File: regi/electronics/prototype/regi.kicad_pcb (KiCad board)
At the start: 2 copper layers, 70.3 x 67.5 mm, 86 parts, among them J1 USB2UART, J2 1.47 IPS LCD, J3 ConnBattery, J4 RTD_PT100, Q1 SS8050, Q2 SS8050, Q3 SS8050, Q5 SS8050, SW1 RST, SW2 IN1, SW3 Boot, SW4 IN2, SW5 IN4, SW6 IN4, SW7 IN5, U1 CH340C, U2 ESP32-S3-WROOM-1, U3 TPS63001_SEPIC_3V3, U4 MAX31865xTP, U5 BQ24075RGT_DPPM, U7 BQ27421YZFR-G1A

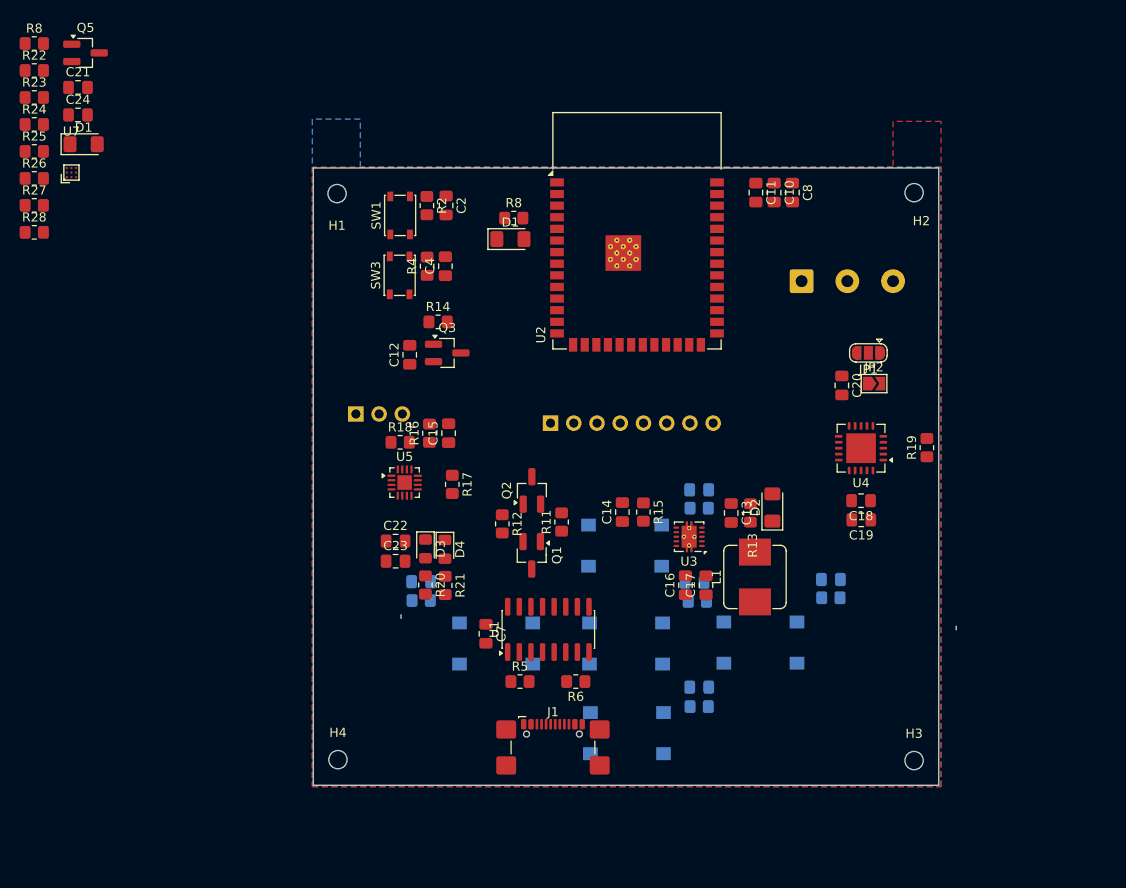
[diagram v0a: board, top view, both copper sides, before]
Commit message: feat(regi): finished rough routing
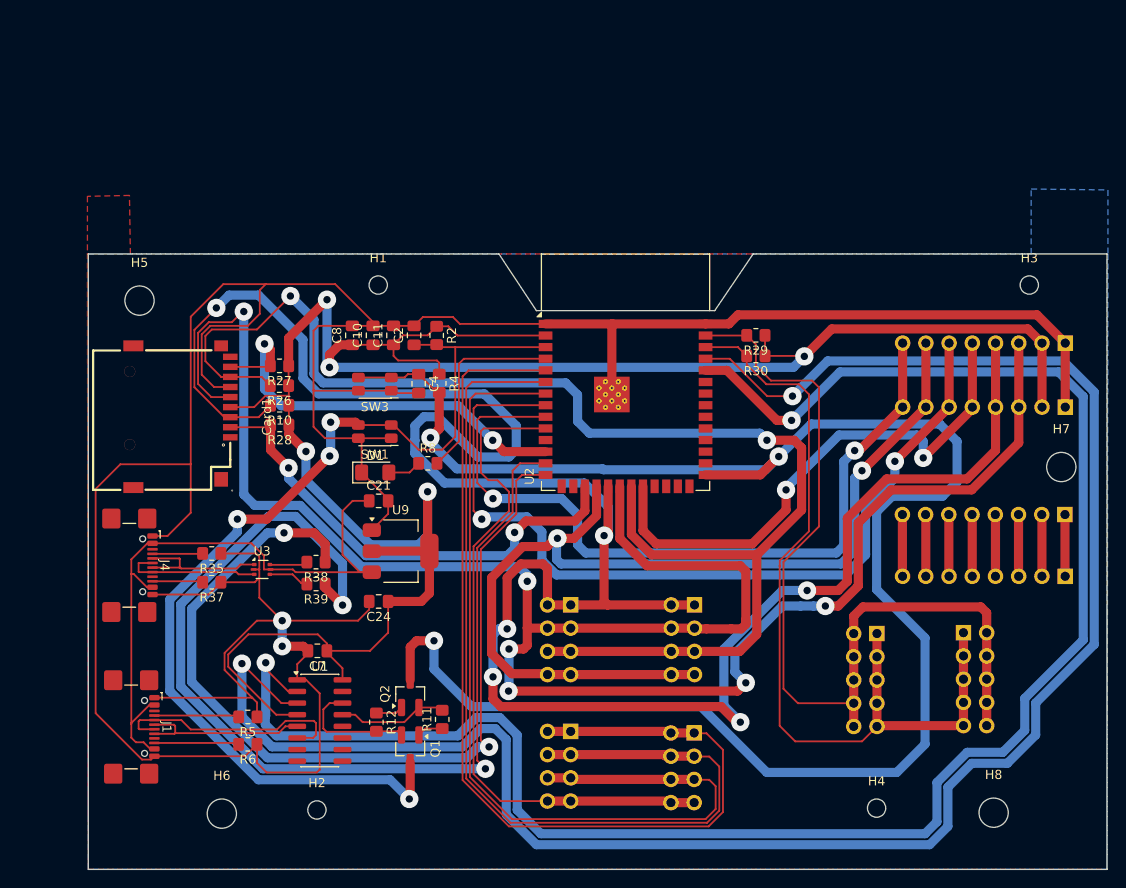
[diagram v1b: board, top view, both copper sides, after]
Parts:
- removed C1, C12, C18, C19, C20, C3, C5, C6, C9: 100nF, Capacitor_SMD:C_0805_2012Metric_Pad1.18x1.45mm_HandSolder
- removed C13, C16, C17: 10uF, Capacitor_SMD:C_0805_2012Metric_Pad1.18x1.45mm_HandSolder
- removed C14: 0.1uF, Capacitor_SMD:C_0805_2012Metric_Pad1.18x1.45mm_HandSolder
- removed C15: 1uF, Capacitor_SMD:C_0805_2012Metric_Pad1.18x1.45mm_HandSolder
- removed C22, C23: 4.7uF, Capacitor_SMD:C_0805_2012Metric_Pad1.18x1.45mm_HandSolder
- removed the D1 at (76.5, 65.0)
- removed the D1 at (123.2, 75.4)
- removed D2: VDD, LED_SMD:LED_1206_3216Metric_Pad1.42x1.75mm_HandSolder
- removed D3: green, LED_SMD:LED_0805_2012Metric_Pad1.15x1.40mm_HandSolder
- removed D4: red, LED_SMD:LED_0805_2012Metric_Pad1.15x1.40mm_HandSolder
- removed JP1: 3_OR_2_Wire, Jumper:SolderJumper-3_P1.3mm_Open_RoundedPad1.0x1.5mm
- removed JP2: 2_Wire, Jumper:SolderJumper-2_P1.3mm_Open_TrianglePad1.0x1.5mm
- removed L1: 22uH 1A, Inductor_SMD:L_Bourns_SRP7028A_7.3x6.6mm
- removed Q3, Q5: SS8050, Package_TO_SOT_SMD:SOT-23_Handsoldering
- removed R1, R13, R14, R3, R7, R9: 1k, Resistor_SMD:R_0805_2012Metric_Pad1.20x1.40mm_HandSolder
- removed R15: 100, Resistor_SMD:R_0805_2012Metric_Pad1.20x1.40mm_HandSolder
- removed R16: 46.4K, Resistor_SMD:R_0805_2012Metric_Pad1.20x1.40mm_HandSolder
- removed R17: 2K2, Resistor_SMD:R_0805_2012Metric_Pad1.20x1.40mm_HandSolder
- removed R18: 1.13k, Resistor_SMD:R_0805_2012Metric_Pad1.20x1.40mm_HandSolder
- removed R19: 430 1%, Resistor_SMD:R_0805_2012Metric_Pad1.20x1.40mm_HandSolder
- removed R20, R21: 1K5, Resistor_SMD:R_0805_2012Metric_Pad1.20x1.40mm_HandSolder
- removed R22, R23: 4K7, Resistor_SMD:R_0805_2012Metric_Pad1.20x1.40mm_HandSolder
- removed R24: 10k, Resistor_SMD:R_0805_2012Metric_Pad1.20x1.40mm_HandSolder
- removed R25: 10K, Resistor_SMD:R_0805_2012Metric_Pad1.20x1.40mm_HandSolder
- removed the R8 at (71.1, 54.0)
- removed the R8 at (123.5, 73.1)
- removed SW2: IN1, Button_Switch_SMD:SW_SPST_Omron_B3FS-100xP
- removed SW4: IN2, Button_Switch_SMD:SW_SPST_Omron_B3FS-100xP
- removed SW5, SW6: IN4, Button_Switch_SMD:SW_SPST_Omron_B3FS-100xP
- removed SW7: IN5, Button_Switch_SMD:SW_SPST_Omron_B3FS-100xP
- removed U4: MAX31865xTP, Package_DFN_QFN:TQFN-20-1EP_5x5mm_P0.65mm_EP3.25x3.25mm
- removed U5: BQ24075RGT_DPPM, Package_DFN_QFN:VQFN-16-1EP_3x3mm_P0.5mm_EP1.6x1.6mm
- removed U7: BQ27421YZFR-G1A, easyeda2kicad:DSBGA-9_L1.5-W1.5-R3-C3-P0.50-BL
- added Card1: TF PUSH, easyeda2kicad:TF-SMD_TF-PUSH, F.Cu at (87.2, 94.8)
- added D1: Indicator, LED_SMD:LED_1206_3216Metric_Pad1.42x1.75mm_HandSolder, F.Cu at (108.4, 100.9)
- added H5: MountingHole, MountingHole:MountingHole_3.2mm_M3, F.Cu at (82.6, 82.1)
- added H6: MountingHole, MountingHole:MountingHole_3.2mm_M3, F.Cu at (91.6, 138.2)
- added H7: MountingHole, MountingHole:MountingHole_3.2mm_M3, F.Cu at (183.4, 100.3)
- added H8: MountingHole, MountingHole:MountingHole_3.2mm_M3, F.Cu at (176.0, 138.1)
- added J10: PinHeaderSPI2, Connector_PinHeader_2.54mm:PinHeader_2x04_P2.54mm_Vertical, B.Cu at (129.8, 129.2)
- added J11: PinSocketSPI1, Connector_PinHeader_2.54mm:PinHeader_2x04_P2.54mm_Vertical, B.Cu at (143.3, 115.4)
- added J12: PinSocketSPI2, Connector_PinHeader_2.54mm:PinHeader_2x04_P2.54mm_Vertical, B.Cu at (143.2, 129.4)
- added J5: lcd jumper, Connector_PinHeader_2.54mm:PinHeader_1x08_P2.54mm_Vertical, B.Cu at (183.8, 86.8)
- added J6: lcd jumper, Connector_PinHeader_2.54mm:PinHeader_1x08_P2.54mm_Vertical, B.Cu at (183.8, 112.2)
- added J7: lcd jumper, Connector_PinHeader_2.54mm:PinHeader_1x08_P2.54mm_Vertical, B.Cu at (183.8, 105.5)
- added J8: PinSocketI2C, Connector_PinSocket_2.54mm:PinSocket_2x05_P2.54mm_Vertical, B.Cu at (172.7, 118.4)
- added J9: PinHeaderSPI1, Connector_PinHeader_2.54mm:PinHeader_2x04_P2.54mm_Vertical, B.Cu at (129.8, 115.4)
- added R29: 4K7, Resistor_SMD:R_0805_2012Metric_Pad1.20x1.40mm_HandSolder, F.Cu at (150.0, 85.9)
- added R30: 4K7, Resistor_SMD:R_0805_2012Metric_Pad1.20x1.40mm_HandSolder, F.Cu at (150.0, 88.2)
- added R35: 5K1, Resistor_SMD:R_0805_2012Metric_Pad1.20x1.40mm_HandSolder, F.Cu at (90.5, 109.8)
- added R37: 5K1, Resistor_SMD:R_0805_2012Metric_Pad1.20x1.40mm_HandSolder, F.Cu at (90.5, 112.9)
- added R38: 22 / 33, Resistor_SMD:R_0805_2012Metric_Pad1.20x1.40mm_HandSolder, F.Cu at (101.9, 110.7)
- added R39: 22 / 33, Resistor_SMD:R_0805_2012Metric_Pad1.20x1.40mm_HandSolder, F.Cu at (101.9, 113.1)
- added R8: 1k, Resistor_SMD:R_0805_2012Metric_Pad1.20x1.40mm_HandSolder, F.Cu at (114.1, 99.9)
- added U9: AMS1117-3.3, Package_TO_SOT_SMD:SOT-223-3_TabPin2, F.Cu at (111.2, 109.5)
- C21: value 0.47uF -> 22uF
- C24: value 100nF -> 22uF
- J3: value ConnBattery -> PinHeaderI2C; footprint Connector_PinHeader_2.54mm:PinHeader_1x03_P2.54mm_Vertical -> Connector_PinHeader_2.54mm:PinHeader_2x05_P2.54mm_Vertical
- J4: value RTD_PT100 -> USB2UART; footprint TerminalBlock_Phoenix:TerminalBlock_Phoenix_PT-1,5-3-5.0-H_1x03_P5.00mm_Horizontal -> Connector_USB:USB_C_Receptacle_GCT_USB4110; moved to F.Cu
- R10: value 1k -> 51k; moved to F.Cu
- R26: value 10K -> 51k
- R27: value 1k -> 51k
- R28: value 10k -> 51k
- SW1, SW3: footprint Button_Switch_SMD:SW_SPST_PTS810 -> Button_Switch_SMD:SW_SPST_EVQP7A
- U3: value TPS63001_SEPIC_3V3 -> USBLC6-2P6; footprint Package_SON:Texas_DRC0010J_ThermalVias -> Package_TO_SOT_SMD:SOT-666
- moved H2 93.9 mm to (102.0, 137.8)
- moved J4 80.9 mm to (80.3, 111.0), turned to -90 degrees
- moved C24 62.5 mm to (108.8, 115.0), turned to 180 degrees
- moved J3 61.8 mm to (163.2, 118.5), turned to 180 degrees
- moved H4 59.1 mm to (163.2, 137.6)
- moved J2 56.3 mm to (183.8, 93.8), turned to 90 degrees
- moved C21 55.9 mm to (108.8, 104.0)
- moved H3 53.5 mm to (179.9, 80.4)
- moved C8 50.6 mm to (105.9, 85.9), turned to 90 degrees
- moved R10 50.5 mm to (97.9, 93.5), turned to 180 degrees
- moved J1 47.4 mm to (80.5, 128.7), turned to -90 degrees
- moved U3 46.8 mm to (96.0, 111.5), turned to 0 degrees
- moved C10 46.6 mm to (108.1, 85.9), turned to 90 degrees
- moved C11 42.6 mm to (110.4, 85.9), turned to 90 degrees
- moved R6 36.5 mm to (94.4, 130.6)
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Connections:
- C21 pad 1: Net-(U7-VDD) -> VBUS
- C24 pad 1: /GPOUT -> +3.3V
- J3 pad 1: +BATT -> /I2C_SCL
- J3 pad 2: /TS -> /I2C_SDA
- J3 pad 3: GND -> /I2C_SCL
- R10 pad 2: /IN5 -> /MOSI
- R26 pad 1: /GPOUT -> +3.3V
- R26 pad 2: GND -> /MISO
- R27 pad 2: Net-(Q5-C) -> /MMC_INT
- R28 pad 2: Net-(Q5-B) -> /MMC_CS
- U2 pad 10: /IN1 -> /CS2
- U2 pad 11: /IN2 -> unconnected-(U2-IO18-Pad11)
- U2 pad 12: /MAX31865DRDY -> /MMC_INT
- U2 pad 13: /IN3 -> /USB_DM
- U2 pad 14: /IN4 -> /USB_DP
- U2 pad 17: /MAX31865CS -> /MMC_CS
- U2 pad 23: /IN5 -> unconnected-(U2-IO21-Pad23)
- U2 pad 31: Net-(Q3-E) -> unconnected-(U2-IO38-Pad31)
- U2 pad 32: /GPOUT -> unconnected-(U2-IO39-Pad32)
- U3 pad 1: +3.3V -> Net-(J4-D--PadA7)
- U3 pad 2: Net-(U3-L2) -> GND
- U3 pad 3: GND -> Net-(J4-D+-PadA6)
- U3 pad 5: VDD -> VBUS
- U3 pad 6: Net-(U3-EN) -> Net-(R38-Pad2)
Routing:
- net GND: track 0.00 -> 362.0 mm, vias 0 -> 2
- net /MOSI: track 0.00 -> 263.1 mm, vias 0 -> 6
- net +3.3V: track 0.00 -> 247.6 mm, vias 0 -> 5
- net /SCK: track 0.00 -> 239.2 mm, vias 0 -> 6
- net /TXD0: track 0.00 -> 207.5 mm, vias 0 -> 2
- net /RXD0: track 0.00 -> 199.6 mm, vias 0 -> 2
- net /IO0: track 0.00 -> 197.6 mm, vias 0 -> 3
- net /MISO: track 0.00 -> 169.8 mm, vias 0 -> 2
- net /CS: track 0.00 -> 126.7 mm, vias 0 -> 2
- net /MOSI2: track 0.00 -> 125.1 mm
- net /SCK2: track 0.00 -> 119.6 mm
- net /USB_DM: track 0.00 -> 116.0 mm, vias 0 -> 2
- net /MISO2: track 0.00 -> 113.9 mm
- net /EN: track 0.00 -> 113.5 mm, vias 0 -> 4
- net /USB_DP: track 0.00 -> 99.7 mm, vias 0 -> 2
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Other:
- board size 70.3 x 67.5 mm -> 111.4 x 67.3 mm
